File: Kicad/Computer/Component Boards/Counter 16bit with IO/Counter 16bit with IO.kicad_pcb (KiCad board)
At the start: 2 copper layers, 26.7 x 59.7 mm, 22 parts, among them IC1 74LVC573APW,118, IC10 74LVC161PW,112, IC11 74LVC574APW,118, IC12 74LVC574APW,118, IC2 74LVC573APW,118, IC4 74LVC2G04GW-Q100H, IC5 AP7365-33WG-7, IC7 74LVC161PW,112, IC8 74LVC161PW,112, IC9 74LVC161PW,112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

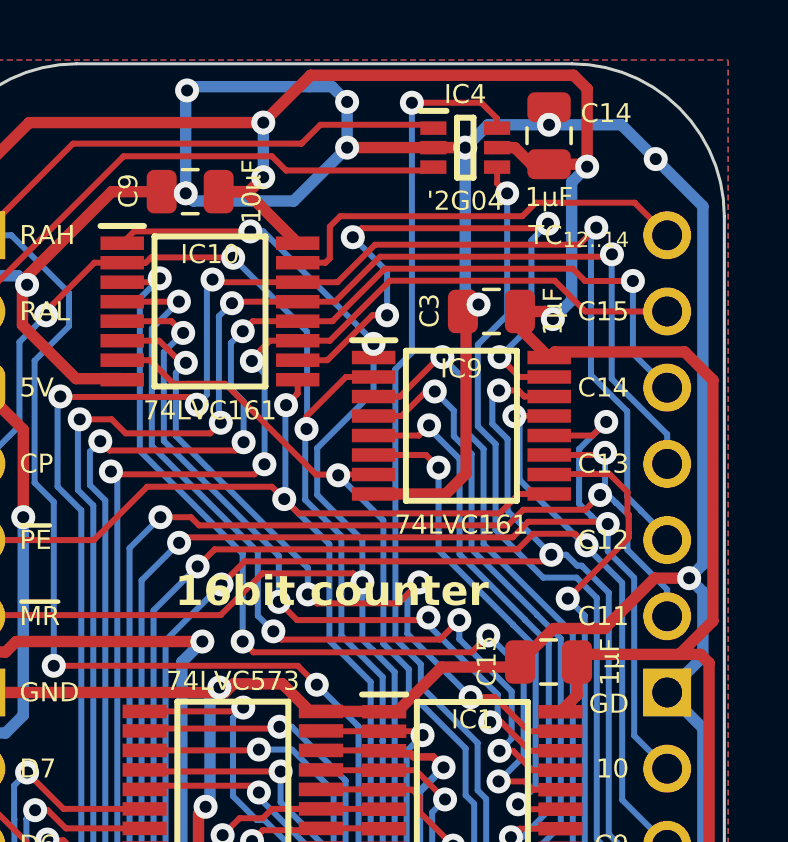
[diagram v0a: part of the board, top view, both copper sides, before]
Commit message: Resized 15mm wide boards and fixed GND pins.  Added GPIO 4bit and PS2 Board.
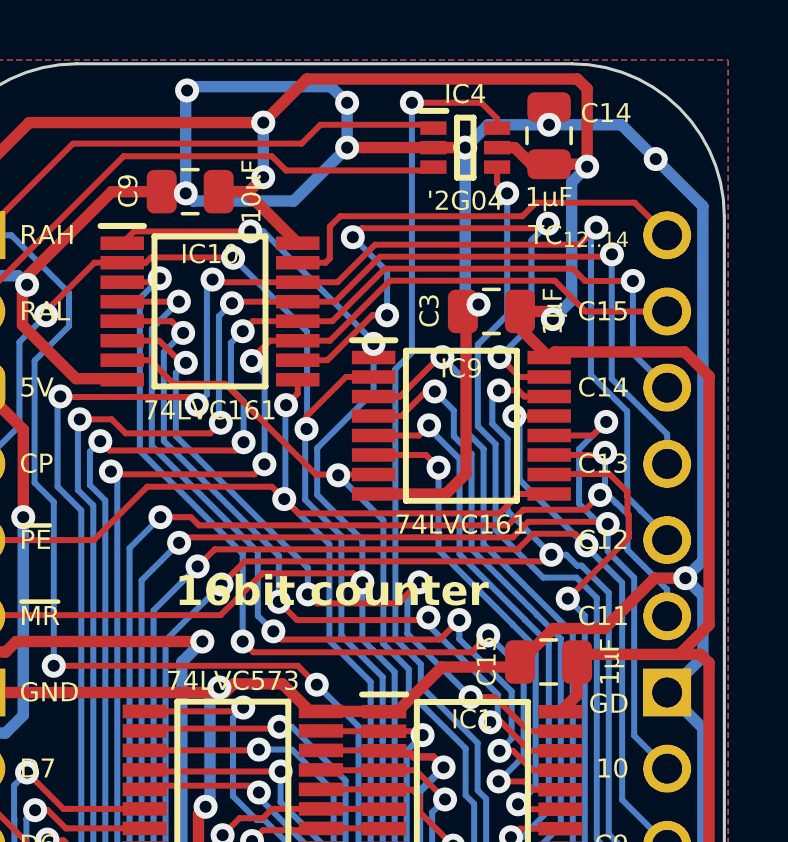
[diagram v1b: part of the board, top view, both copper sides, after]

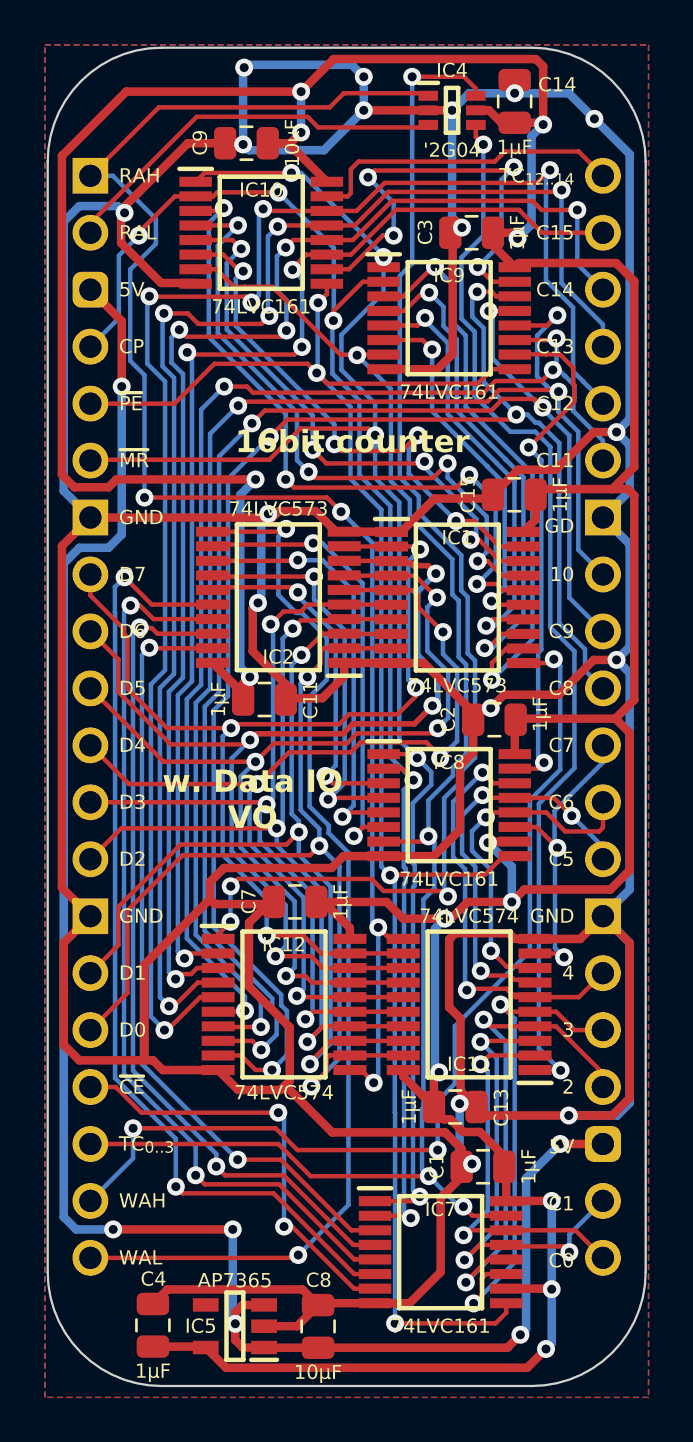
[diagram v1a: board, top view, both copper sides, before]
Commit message: Added terminal count output and latch enable to 16bit and 24bit counters.
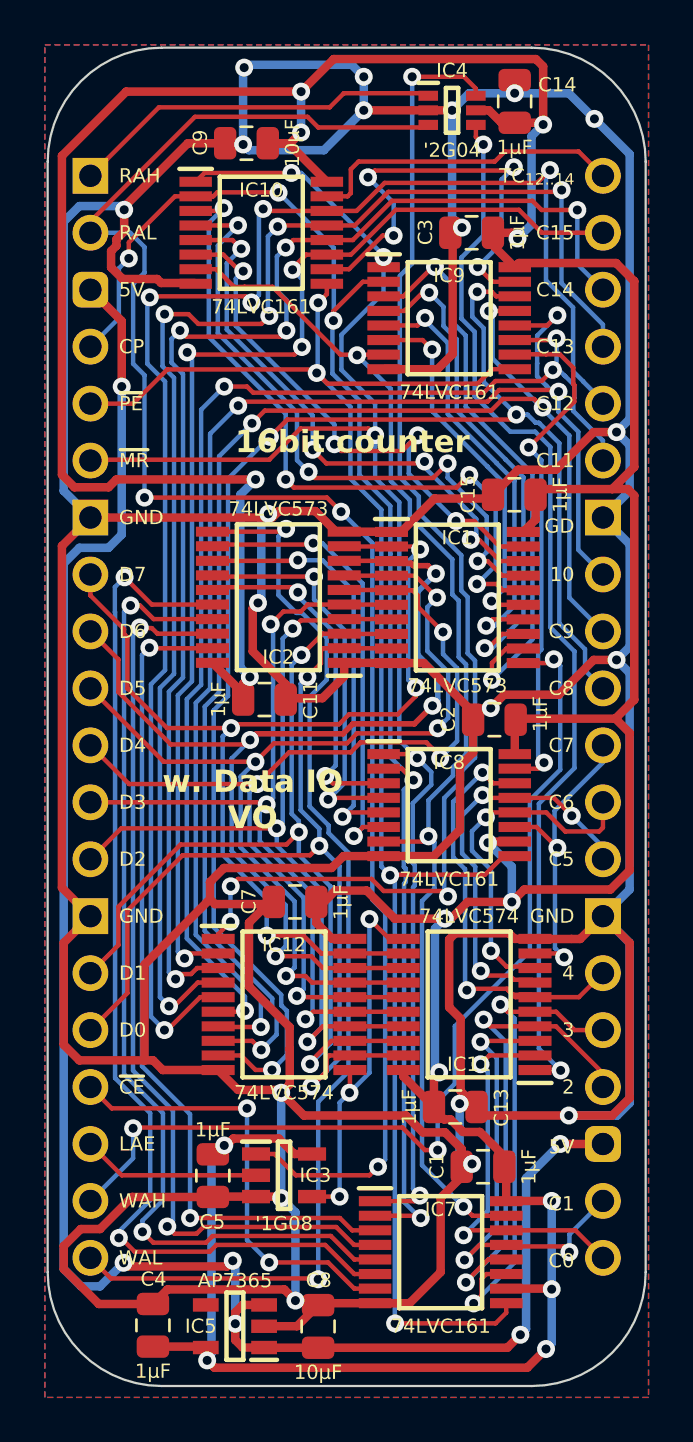
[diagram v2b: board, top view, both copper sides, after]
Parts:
- added C5: 1μF, SamacSys_Parts:C_0805, F.Cu at (94.4, 103.0)
- added IC3: 74LVC1G08GV,125, SamacSys_Parts:SOT95P275X110-5N, F.Cu at (97.5, 103.0)
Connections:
- IC11 pad 11: /Read Address High -> /Latch Address
- IC12 pad 11: /Read Address High -> /Latch Address
- J2 pad 18: /TC_{0..3} -> /Latch Address Enable
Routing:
- net /Read Address Low: track 16.9 -> 76.3 mm, vias 0 -> 3
- net /Read Address High: track 70.2 -> 16.5 mm, vias 4 -> 0
- net /GND: track 314.5 -> 341.4 mm, vias 17 -> 20
- net /Latch Address: track 0.00 -> 16.4 mm, vias 0 -> 3
- net /3.3V: track 191.6 -> 207.4 mm, vias 13 -> 15
- net /TC_{0..3}: track 71.7 -> 55.9 mm, vias 4 -> 3
- net /Latch Address Enable: track 0.00 -> 7.96 mm
- net /LC3: track 43.4 -> 47.6 mm
- net /LC2: track 40.3 -> 44.2 mm
- net /LC1: track 37.6 -> 40.9 mm
- net /LC0: track 35.0 -> 37.8 mm
- net /Write Start Address Low: track 48.2 -> 50.1 mm
- net /5V: track 82.7 -> 84.3 mm
- net /CP: track 68.0 -> 68.6 mm
- net /CE: track 19.2 -> 19.9 mm
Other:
- board text added: "LAE"
- board text removed: "TC_{0..3}"

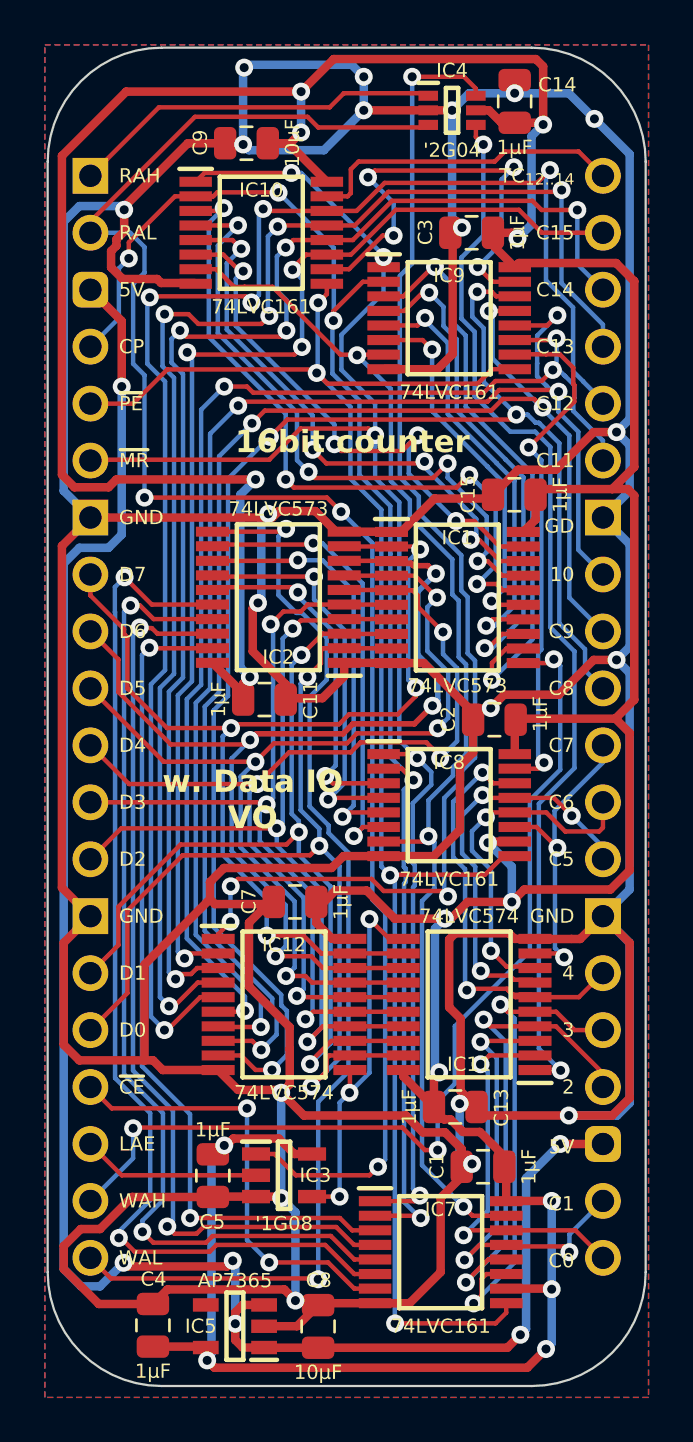
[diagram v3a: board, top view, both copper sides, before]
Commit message: Regenerating some gerbers again with paste layers.
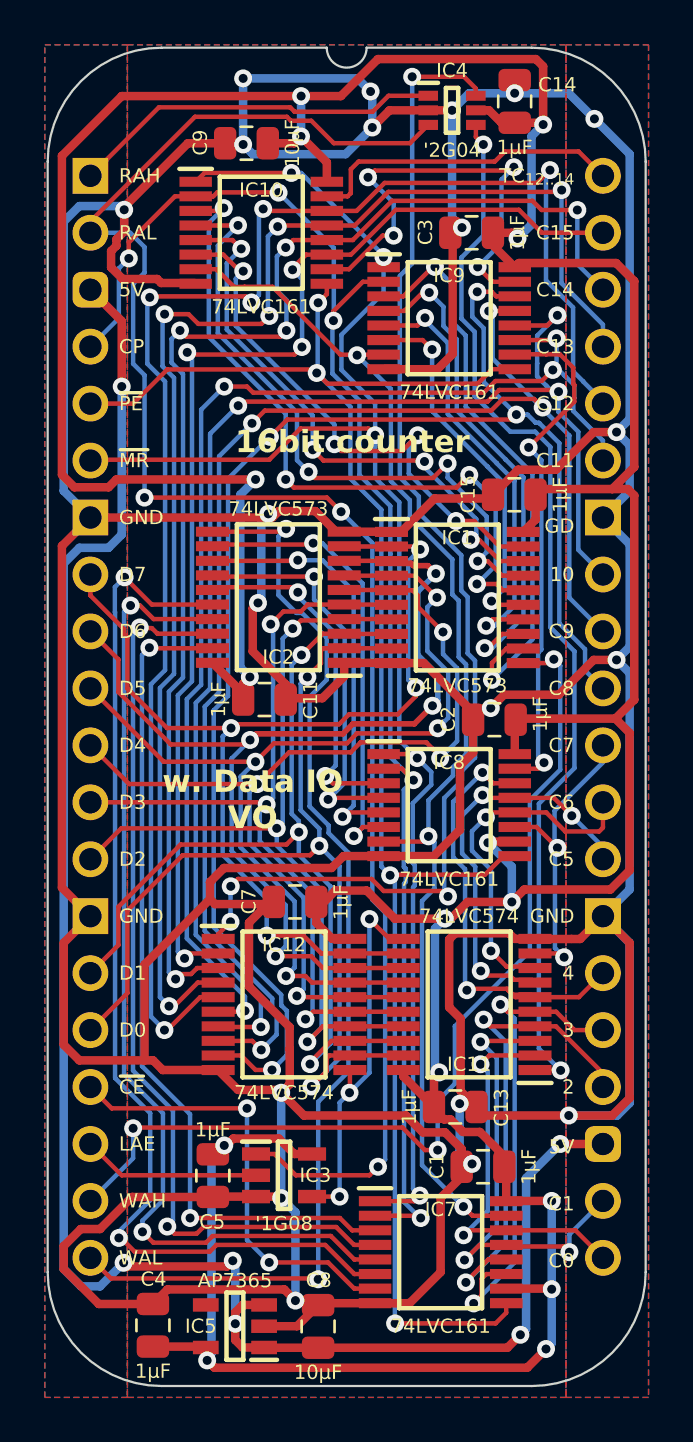
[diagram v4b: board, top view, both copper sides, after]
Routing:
- net /Read Address Low: track 76.3 -> 77.3 mm
- net /3.3V: track 207.4 -> 206.5 mm
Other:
- outline, holes or cut-outs redrawn

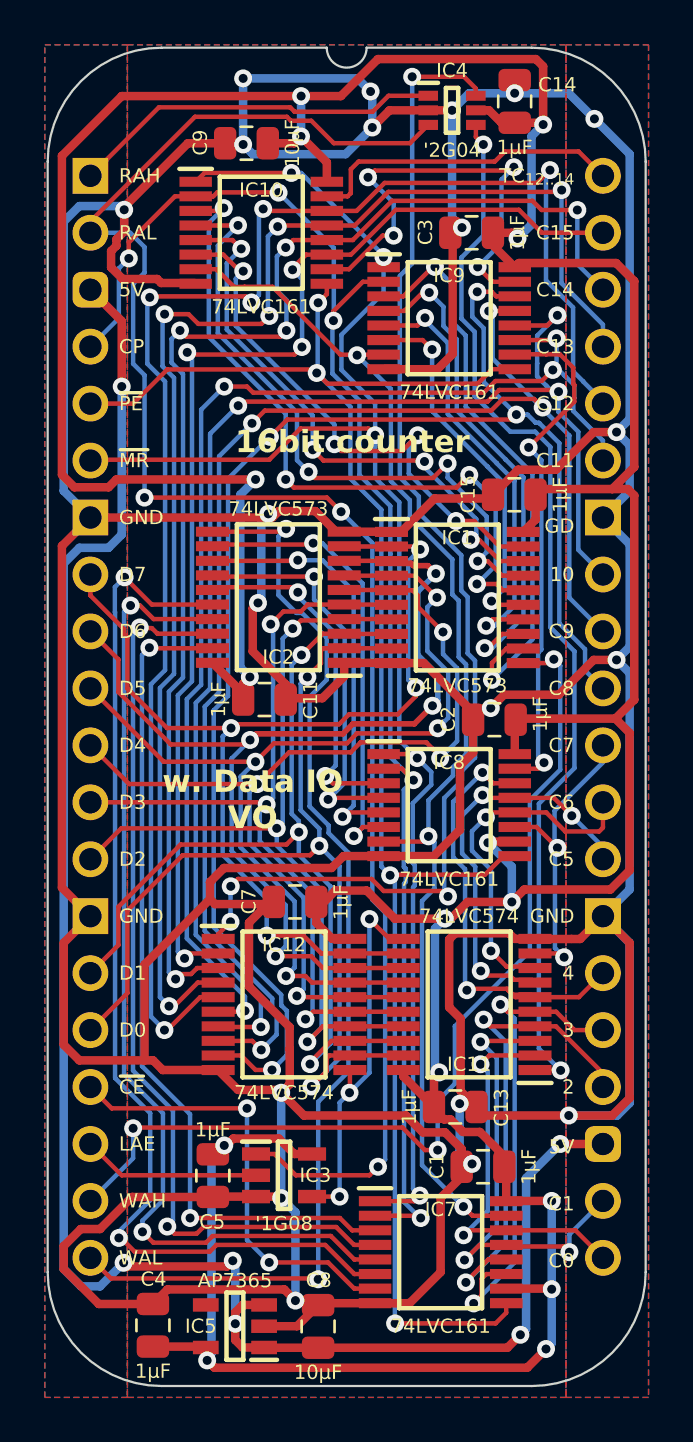
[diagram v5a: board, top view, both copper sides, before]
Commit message: Regenerated a bunch of Gerbers and fixed some component boards.
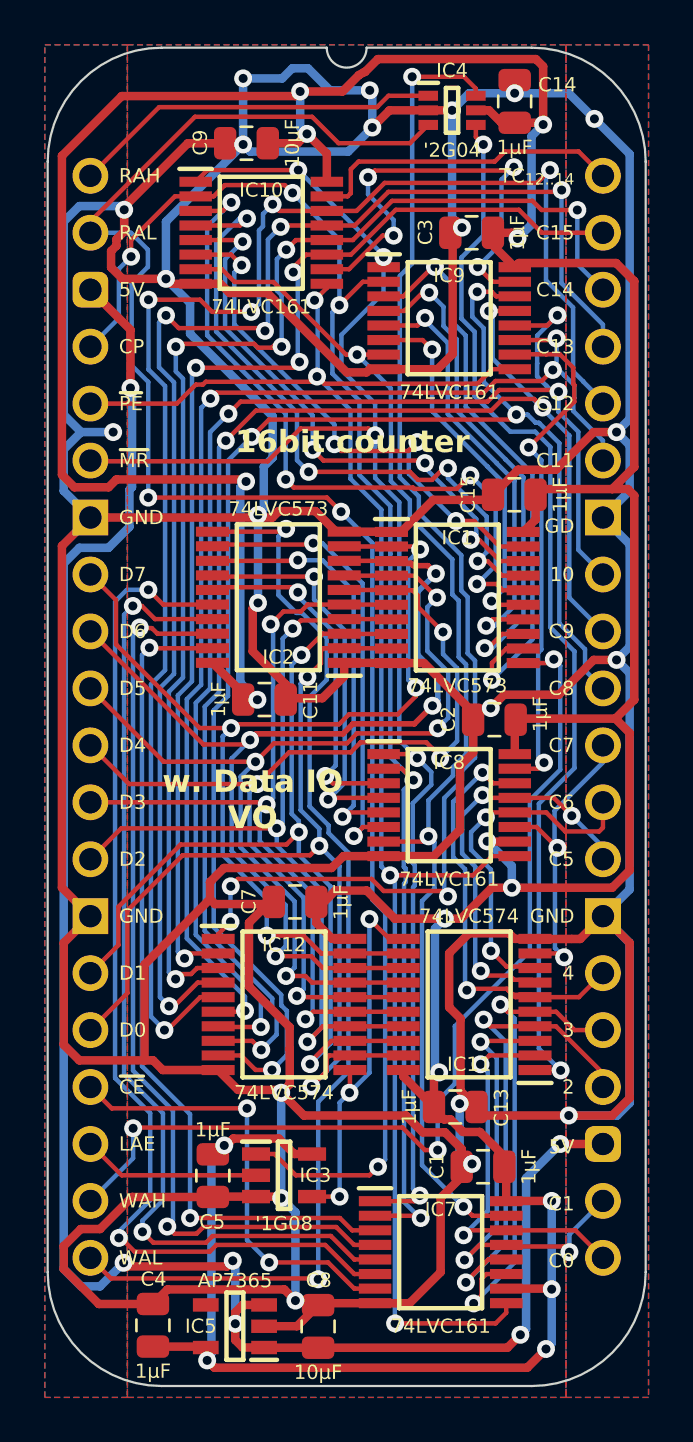
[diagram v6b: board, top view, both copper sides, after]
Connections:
- net /5V renamed 5V
- net /C0 renamed C0
- net /C1 renamed C1
- net /C10 renamed C10
- net /C11 renamed C11
- net /C12 renamed C12
- net /C13 renamed C13
- net /C14 renamed C14
- net /C15 renamed C15
- net /C2 renamed C2
- net /C3 renamed C3
- net /C4 renamed C4
- net /C5 renamed C5
- net /C6 renamed C6
- net /C7 renamed C7
- net /C8 renamed C8
- net /C9 renamed C9
- net /CE renamed CE
- net /CP renamed CP
- net /D0 renamed D0
- net /D1 renamed D1
- net /D2 renamed D2
- net /D3 renamed D3
- net /D4 renamed D4
- net /D5 renamed D5
- net /D6 renamed D6
- net /D7 renamed D7
- net /GND renamed GND
- net /Latch Address Enable renamed Latch Address Enable
- net /Read Address High renamed Read Address High
- net /Read Address Low renamed Read Address Low
- net /TC_{12..15} renamed TC_{12..15}
- net /Write Start Address High renamed Write Start Address High
- net /Write Start Address Low renamed Write Start Address Low
- net /~{MR} renamed ~{MR}
- net /~{PE} renamed ~{PE}
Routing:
- net GND: track 341.5 -> 372.9 mm, vias 20 -> 22
- net /LC13: track 29.1 -> 30.1 mm
- net /LC12: track 31.5 -> 32.5 mm
- net /LC3: track 47.6 -> 46.8 mm
- net D6: track 46.9 -> 46.0 mm
- net D7: track 46.9 -> 46.1 mm
- net C15: track 53.4 -> 52.7 mm

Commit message: Removed some component copper fills.
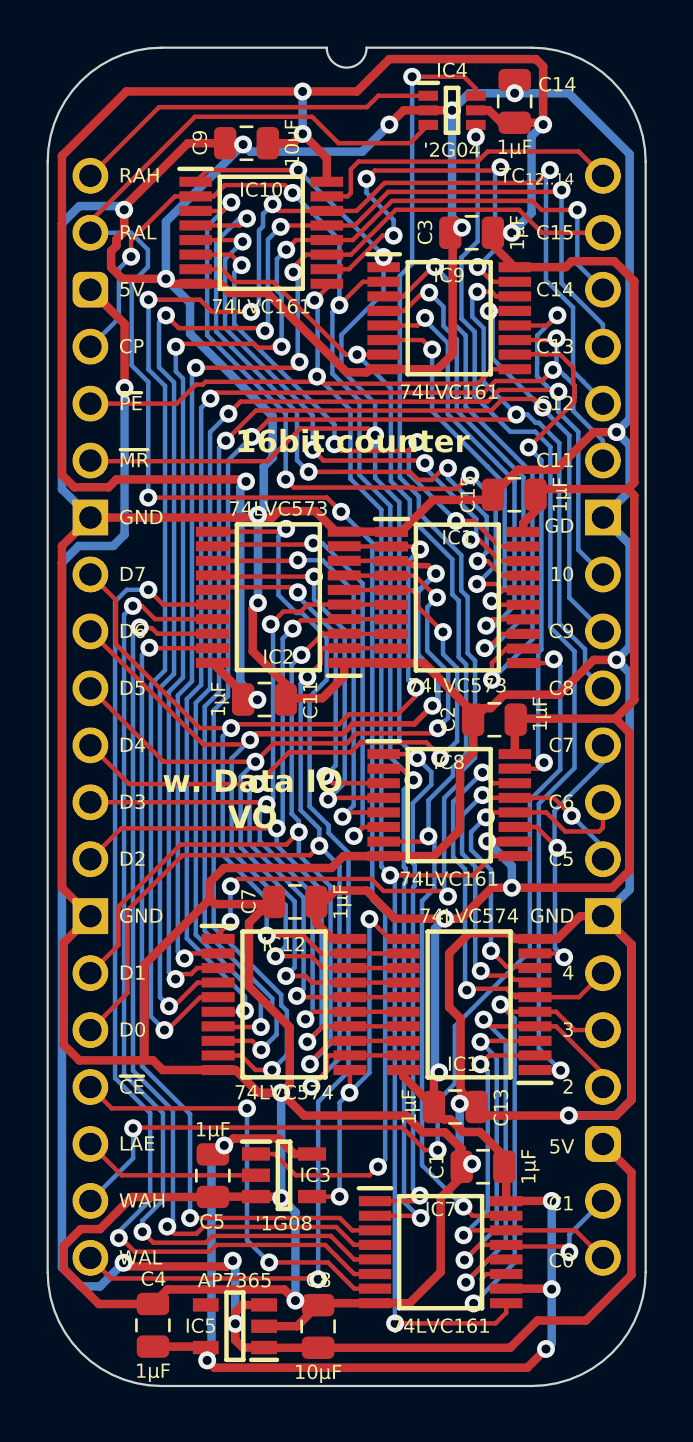
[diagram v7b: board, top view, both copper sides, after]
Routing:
- net GND: track 372.9 -> 360.2 mm, vias 22 -> 17
- net 5V: track 84.7 -> 85.9 mm, vias 6 -> 4
- net /3.3V: track 206.5 -> 205.5 mm
- net /TC_{8..11}: track 20.4 -> 19.6 mm
- removed copper zone on B.Cu, net GND
- removed copper zone on F.Cu, net GND
